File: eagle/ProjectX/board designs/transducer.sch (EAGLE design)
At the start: 20 parts

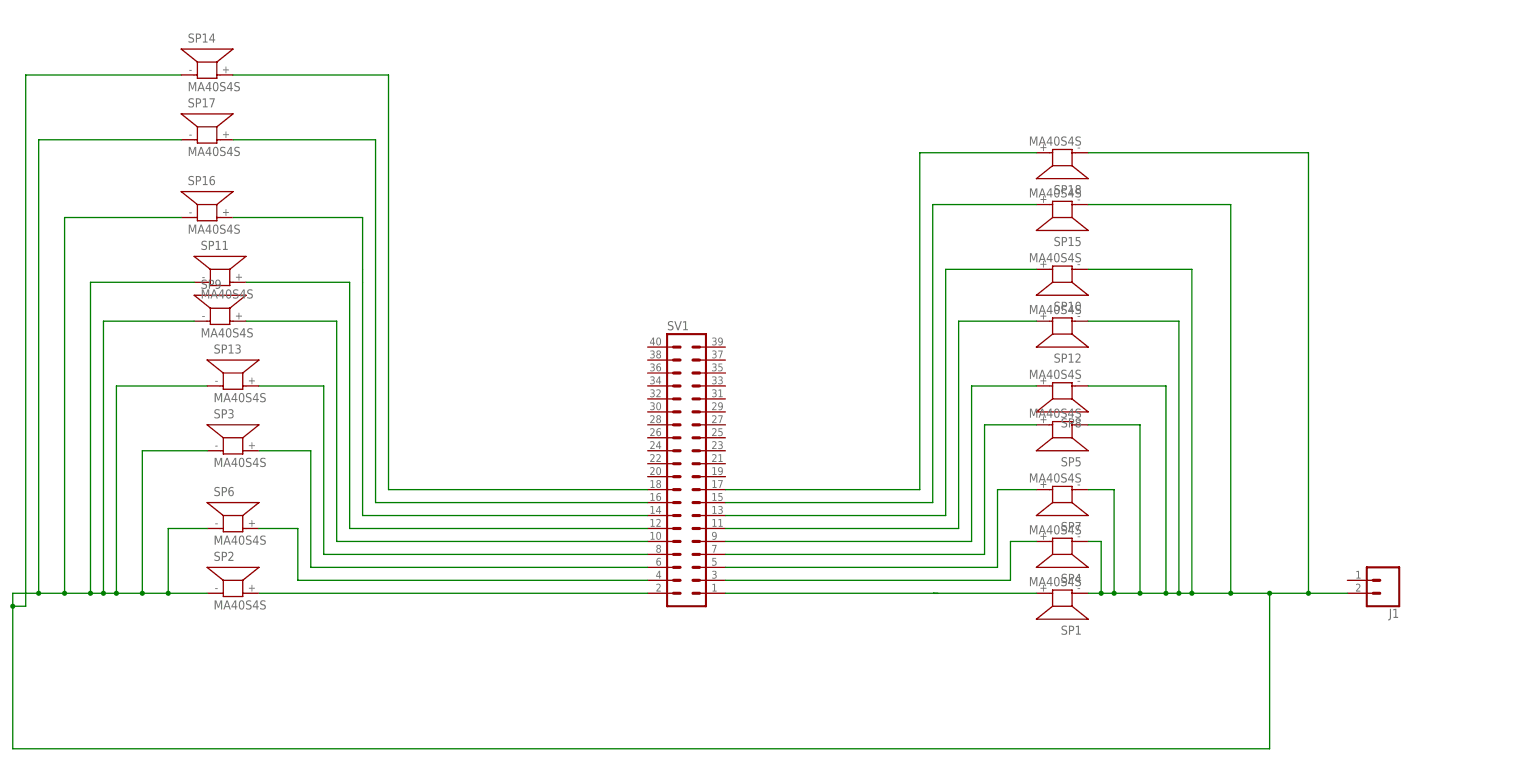
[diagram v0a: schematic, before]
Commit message: Some work on a transducer board
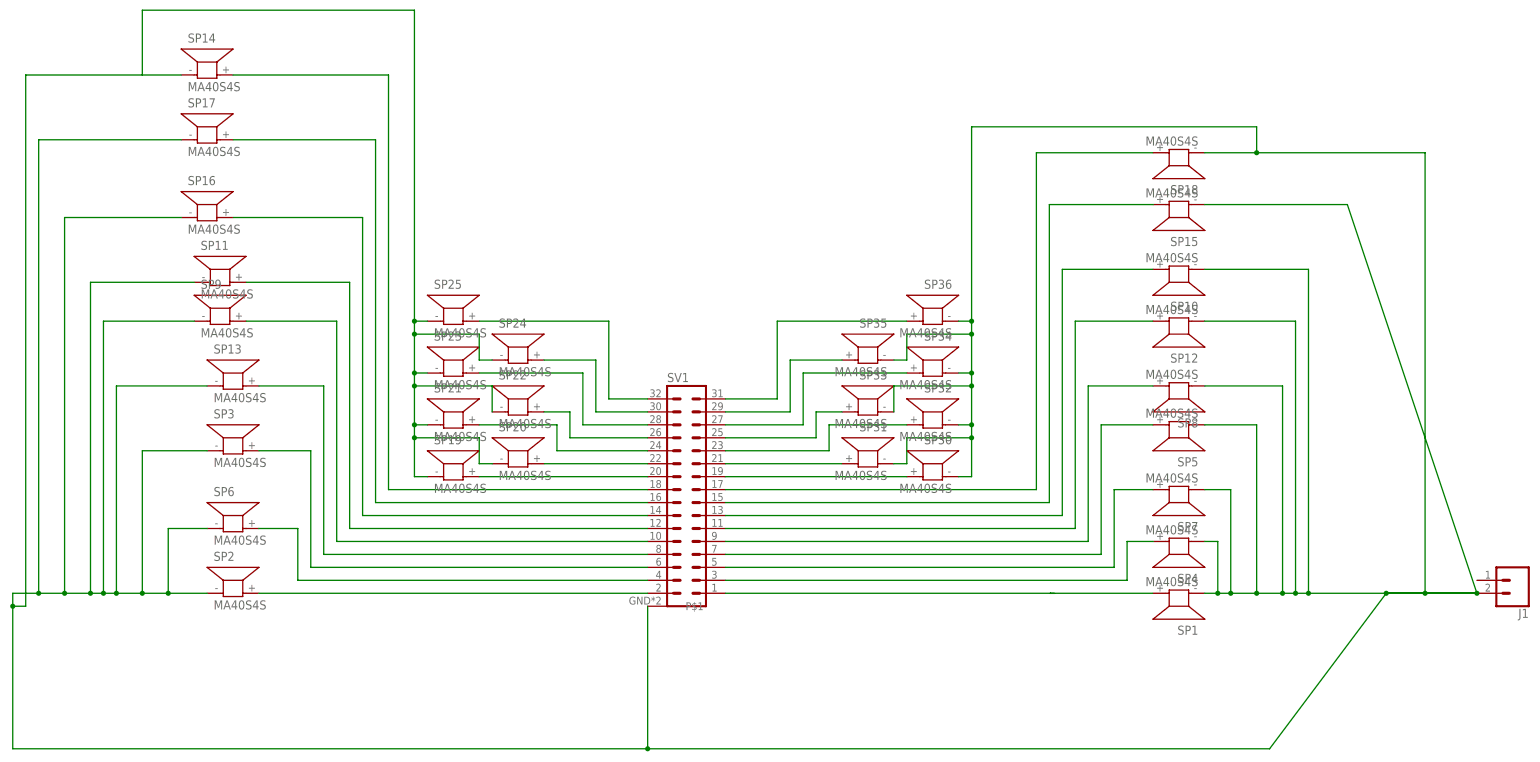
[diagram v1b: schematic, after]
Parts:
- added SP19, SP20, SP21, SP22, SP23, SP24, SP25, SP30, SP31, SP32, SP33, SP34, SP35, SP36: MA40S4S, transducerlibrary:MA40S4S
- SV1: device con-lstb:MA20-2W -> Parts:MA20-2W
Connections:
- removed net N$21: J1.2, SP1.1, SP10.1, SP11.1, SP12.1, SP13.1, SP14.1, SP15.1, SP16.1, SP17.1, SP18.1, SP2.1, SP3.1, SP4.1, SP5.1, SP6.1, SP7.1, SP8.1, SP9.1
- new net GND: J1.2, SP1.1, SP10.1, SP11.1, SP12.1, SP13.1, SP14.1, SP15.1, SP16.1, SP17.1, SP18.1, SP19.1, SP2.1, SP20.1, SP21.1, SP22.1, SP23.1, SP24.1, SP25.1, SP3.1, SP30.1, SP31.1, SP32.1, SP33.1, SP34.1, SP35.1, SP36.1, SP4.1, SP5.1, SP6.1, SP7.1, SP8.1, SP9.1, SV1.P$1
- new net N$10: SP19.2, SV1.20
- new net N$22: SP20.2, SV1.22
- new net N$23: SP21.2, SV1.24
- new net N$24: SP22.2, SV1.26
- new net N$25: SP23.2, SV1.28
- new net N$26: SP24.2, SV1.30
- new net N$27: SP25.2, SV1.32
- new net N$28: SP30.2, SV1.19
- new net N$29: SP31.2, SV1.21
- new net N$30: SP32.2, SV1.23
- new net N$31: SP33.2, SV1.25
- new net N$32: SP34.2, SV1.27
- new net N$33: SP35.2, SV1.29
- new net N$34: SP36.2, SV1.31
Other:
- moved on the sheet: J1, SP1, SP10, SP12, SP15, SP18, SP4, SP5, SP7, SP8
